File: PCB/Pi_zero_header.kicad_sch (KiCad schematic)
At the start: 95 parts, among them J1 Raspberry_Pi_2_3, J2 USB_C_Receptacle_USB2.0, J3 Screw_Terminal_01x02, J4 Screw_Terminal_01x02, SW1 SW_Push, U1 RP2040, U2 W25Q128JVS, U3 TB6612FNG, U4 TPS630701RNMR, U5 TPS630701RNMR, U6 PQ25792RQMR, Y1 Crystal

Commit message: Hopefully done schema
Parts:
- removed C17, C37, C38, C39, C40: 10u, symbol Device:C
- added J5: Conn_02x04_Top_Bottom, Connector_PinHeader_2.54mm:PinHeader_2x04_P2.54mm_Horizontal, symbol Connector_Generic:Conn_02x04_Top_Bottom
- added J7: Conn_01x04, Connector_PinHeader_2.54mm:PinHeader_1x04_P2.54mm_Horizontal, symbol Connector_Generic:Conn_01x04
- added J8: Conn_02x03_Top_Bottom, Connector_PinHeader_2.54mm:PinHeader_2x03_P2.54mm_Horizontal, symbol Connector_Generic:Conn_02x03_Top_Bottom
- added J9: Conn_01x02, Connector_PinHeader_2.54mm:PinHeader_1x02_P2.54mm_Horizontal, symbol Connector_Generic:Conn_01x02
- added SW2: SW_Push, Button_Switch_SMD:SW_Push_1P1T_NO_Vertical_Wuerth_434133025816, symbol Switch:SW_Push
- added SW3: SW_SPST, Button_Switch_THT:SW_DIP_SPSTx01_Piano_10.8x4.1mm_W7.62mm_P2.54mm, symbol Switch:SW_SPST
- C36: value 10u -> 47u
- R2: value R -> 10k
- Y1: value Crystal -> 12M
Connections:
- net +3V3: now also J5.1 (Pin_1), J5.5 (Pin_5)
- net +5V: now also J7.1 (Pin_1), J8.2 (Pin_2), J8.5 (Pin_5)
- net GND: now also J5.2 (Pin_2), J5.6 (Pin_6), J7.2 (Pin_2), J8.3 (Pin_3), J8.6 (Pin_6), J9.2 (Pin_2), SW2.1
- net SCL_PWR: now also U1.4 (GPIO2)
- net SDA_PWR: now also U1.5 (GPIO3)
- net VDD: now also SW3.2 (B); no longer C35.1, C36.1, U6.25 (SYS)
- net MOSI_RPi: now reaches U1.11 (GPIO8)
- net MOSI_RPi: now also J1.19 (MOSI0/GPIO10)
- net SCLK_RPi: now reaches U1.12 (GPIO9)
- net SCLK_RPi: now also J1.23 (SCLK0/GPIO11)
- net at U1.2 (GPIO0): now also J5.3 (Pin_3), J5.7 (Pin_7)
- net at U1.26 (RUN): now also SW2.2
- net at U1.28 (GPIO17): now also J8.4 (Pin_4)
- net at U1.29 (GPIO18): now also J8.1 (Pin_1)
- net at U1.3 (GPIO1): now also J5.4 (Pin_4), J5.8 (Pin_8)
- net PWMA: now reaches U1.30 (GPIO19)
- net PWMA: now also U3.23 (PWMA)
- net PWMB: now reaches U1.31 (GPIO20)
- net PWMB: now also U3.15 (PWMB)
- net AIN1: now reaches U1.32 (GPIO21)
- net AIN1: now also U3.21 (AIN1)
- net AIN2: now reaches U1.34 (GPIO22)
- net AIN2: now also U3.22 (AIN2)
- net BIN1: now reaches U1.35 (GPIO23)
- net BIN1: now also U3.17 (BIN1)
- net BIN2: now reaches U1.36 (GPIO24)
- net BIN2: now also U3.16 (BIN2)
- net STBY_N: now reaches U1.37 (GPIO25)
- net STBY_N: now also U3.19 (STBY)
- net QSPI_SS: now reaches U1.56 (QSPI_SS)
- net QSPI_SS: now also R1.2, R2.2, U2.1 (~{CS})
- net CE_N_PWR: now reaches U1.6 (GPIO4)
- net CE_N_PWR: now also U6.13 (CE_N)
- net QON_N_PWR: now reaches U1.7 (GPIO5)
- net QON_N_PWR: now also U6.12 (QON_N)
- net CE_N_RPI: now reaches U1.8 (GPIO6)
- net CE_N_RPI: now also J1.24 (~{CE0}/GPIO8)
- net MISO_RPi: now reaches U1.9 (GPIO7)
- net MISO_RPi: now also J1.21 (MISO0/GPIO9)
- net +BATT: now reaches C29.1, C30.1, R6.2, U6.22 (BAT), U6.23 (BAT)
- net +BATT: now also J9.1 (Pin_1)
- net at J1.32 (PWM0/GPIO12): now also J7.3 (Pin_3)
- net at J1.33 (PWM1/GPIO13): now also J7.4 (Pin_4)
- new net: C35.1, C36.1, SW3.1 (A), U6.25 (SYS)
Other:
- note added: "AUDIO"
- note added: "BATTERY"
- note added: "BUCK-BOOST"
- note added: "CHARGER"
- note added: "CRYSTAL"
- note added: "FLASH"
- note added: "I2C"
- note added: "MOTORS"
- note added: "RP2040"
- note added: "RPI ZERO 2"
- note added: "SERVOS"
- note added: "USB-C"
- moved on the sheet: C1, C10, C11, C12, C13, C14, C15, C16, C18, C19, C2, C20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

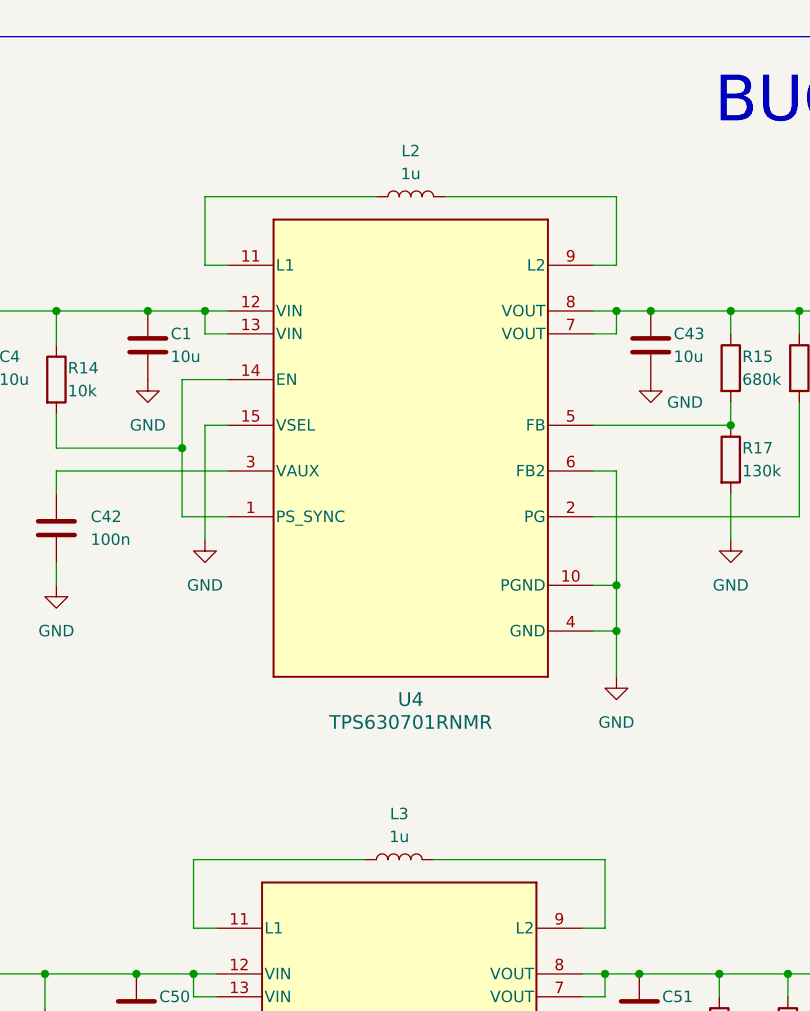
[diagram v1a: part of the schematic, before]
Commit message: Added footprints
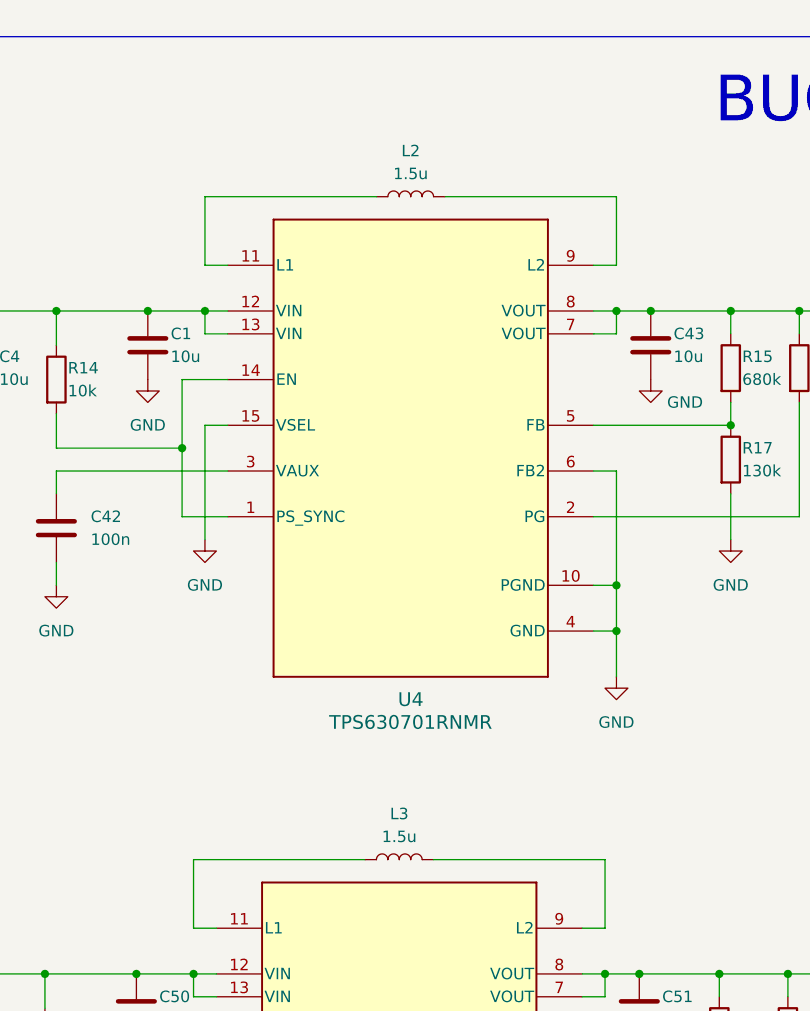
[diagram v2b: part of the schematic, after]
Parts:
- C1, C10, C11, C12, C13, C14, C15, C16, C18, C19, C2, C20, C21, C22, C23, C24, C25, C26, C27, C28, C29, C3, C30, C31, C32, C33, C34, C35, C36, C4, C41, C42, C43, C44, C45, C46, C47, C48, C49, C5, C50, C51, C52, C53, C54, C6, C7, C8, C9: footprint (none) -> Capacitor_SMD:C_0603_1608Metric
- D1: footprint (none) -> LED_SMD:LED_0603_1608Metric
- L1: footprint (none) -> Inductor_SMD:L_0805_2012Metric
- L2, L3: value 1u -> 1.5u; footprint (none) -> Inductor_SMD:L_0805_2012Metric
- R1, R10, R11, R12, R13, R14, R15, R16, R17, R18, R19, R2, R20, R21, R3, R4, R5, R6, R7, R8, R9: footprint (none) -> Resistor_SMD:R_0603_1608Metric
- Y1: footprint (none) -> Crystal:Crystal_SMD_HC49-SD

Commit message: I relized I fucked up...
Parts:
- added D2: LED, LED_SMD:LED_0402_1005Metric, symbol Device:LED
- added J6: Conn_01x07, Connector_PinHeader_2.54mm:PinHeader_1x07_P2.54mm_Vertical, symbol Connector_Generic:Conn_01x07
- added R22: 3k3, Resistor_SMD:R_0402_1005Metric, symbol Device:R
- C1, C10, C11, C12, C13, C14, C15, C16, C18, C19, C2, C20, C21, C22, C23, C24, C25, C26, C27, C28, C29, C3, C30, C31, C32, C33, C34, C35, C36, C4, C41, C42, C43, C44, C45, C46, C47, C48, C49, C5, C50, C51, C52, C53, C54, C6, C7, C8, C9: footprint Capacitor_SMD:C_0603_1608Metric -> Capacitor_SMD:C_0402_1005Metric
- D1: footprint LED_SMD:LED_0603_1608Metric -> LED_SMD:LED_0402_1005Metric
- J5: footprint Connector_PinHeader_2.54mm:PinHeader_2x04_P2.54mm_Horizontal -> Connector_PinHeader_2.54mm:PinHeader_2x04_P2.54mm_Vertical
- J7: footprint Connector_PinHeader_2.54mm:PinHeader_1x04_P2.54mm_Horizontal -> Connector_PinHeader_2.54mm:PinHeader_1x04_P2.54mm_Vertical
- J8: footprint Connector_PinHeader_2.54mm:PinHeader_2x03_P2.54mm_Horizontal -> Connector_PinHeader_2.54mm:PinHeader_2x03_P2.54mm_Vertical
- J9: footprint Connector_PinHeader_2.54mm:PinHeader_1x02_P2.54mm_Horizontal -> Connector_PinHeader_2.54mm:PinHeader_1x02_P2.54mm_Vertical
- R1, R10, R11, R12, R13, R14, R15, R16, R17, R18, R19, R2, R20, R21, R3, R4, R5, R6, R7, R8, R9: footprint Resistor_SMD:R_0603_1608Metric -> Resistor_SMD:R_0402_1005Metric
- SW3: footprint Button_Switch_THT:SW_DIP_SPSTx01_Piano_10.8x4.1mm_W7.62mm_P2.54mm -> Button_Switch_THT:SW_CuK_OS102011MA1QN1_SPDT_Angled
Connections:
- net +3V3: now also J6.1 (Pin_1)
- net GND: now also J6.2 (Pin_2), R22.2
- net at U1.13 (GPIO10): now also J6.3 (Pin_3)
- net at U1.14 (GPIO11): now also J6.4 (Pin_4)
- net at U1.15 (GPIO12): now also J6.5 (Pin_5)
- net at U1.16 (GPIO13): now also J6.6 (Pin_6)
- net at U1.17 (GPIO14): now also J6.7 (Pin_7)
- net at U1.18 (GPIO15): now also D2.1 (K)
- new net: D2.2 (A), R22.1
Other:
- note added: "SPI"
- moved on the sheet: J5

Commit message: Updated PCB design
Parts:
- removed J7: Conn_01x04, Connector_PinHeader_2.54mm:PinHeader_1x04_P2.54mm_Vertical, symbol Connector_Generic:Conn_01x04
- removed Y1: 12M, Crystal:Crystal_SMD_HC49-SD, symbol Device:Crystal
- added Y2: 12M, Crystal:Crystal_SMD_3225-4Pin_3.2x2.5mm, symbol Device:Crystal_GND24
- C1, C19, C21, C24, C25, C27, C28, C29, C30, C4, C41, C43, C47, C48, C50, C51: footprint Capacitor_SMD:C_0402_1005Metric -> Capacitor_SMD:C_0805_2012Metric
- C2, C3: value 27p -> 15p
- C34, C44, C45, C46, C52, C53, C54: footprint Capacitor_SMD:C_0402_1005Metric -> Capacitor_SMD:C_0603_1608Metric
- C36: footprint Capacitor_SMD:C_0402_1005Metric -> Capacitor_SMD:C_1206_3216Metric
- L1, L2, L3: footprint Inductor_SMD:L_0805_2012Metric -> Inductor_SMD:L_1008_2520Metric
- SW3: footprint Button_Switch_THT:SW_CuK_OS102011MA1QN1_SPDT_Angled -> Button_Switch_SMD:SW_SPDT_PCM12
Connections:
- net GND: now also Y2.2, Y2.4
- net XIN: now also Y2.3
- net at C3.1, R5.1: now also Y2.1
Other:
- note removed: "AUDIO"
- moved on the sheet: R5

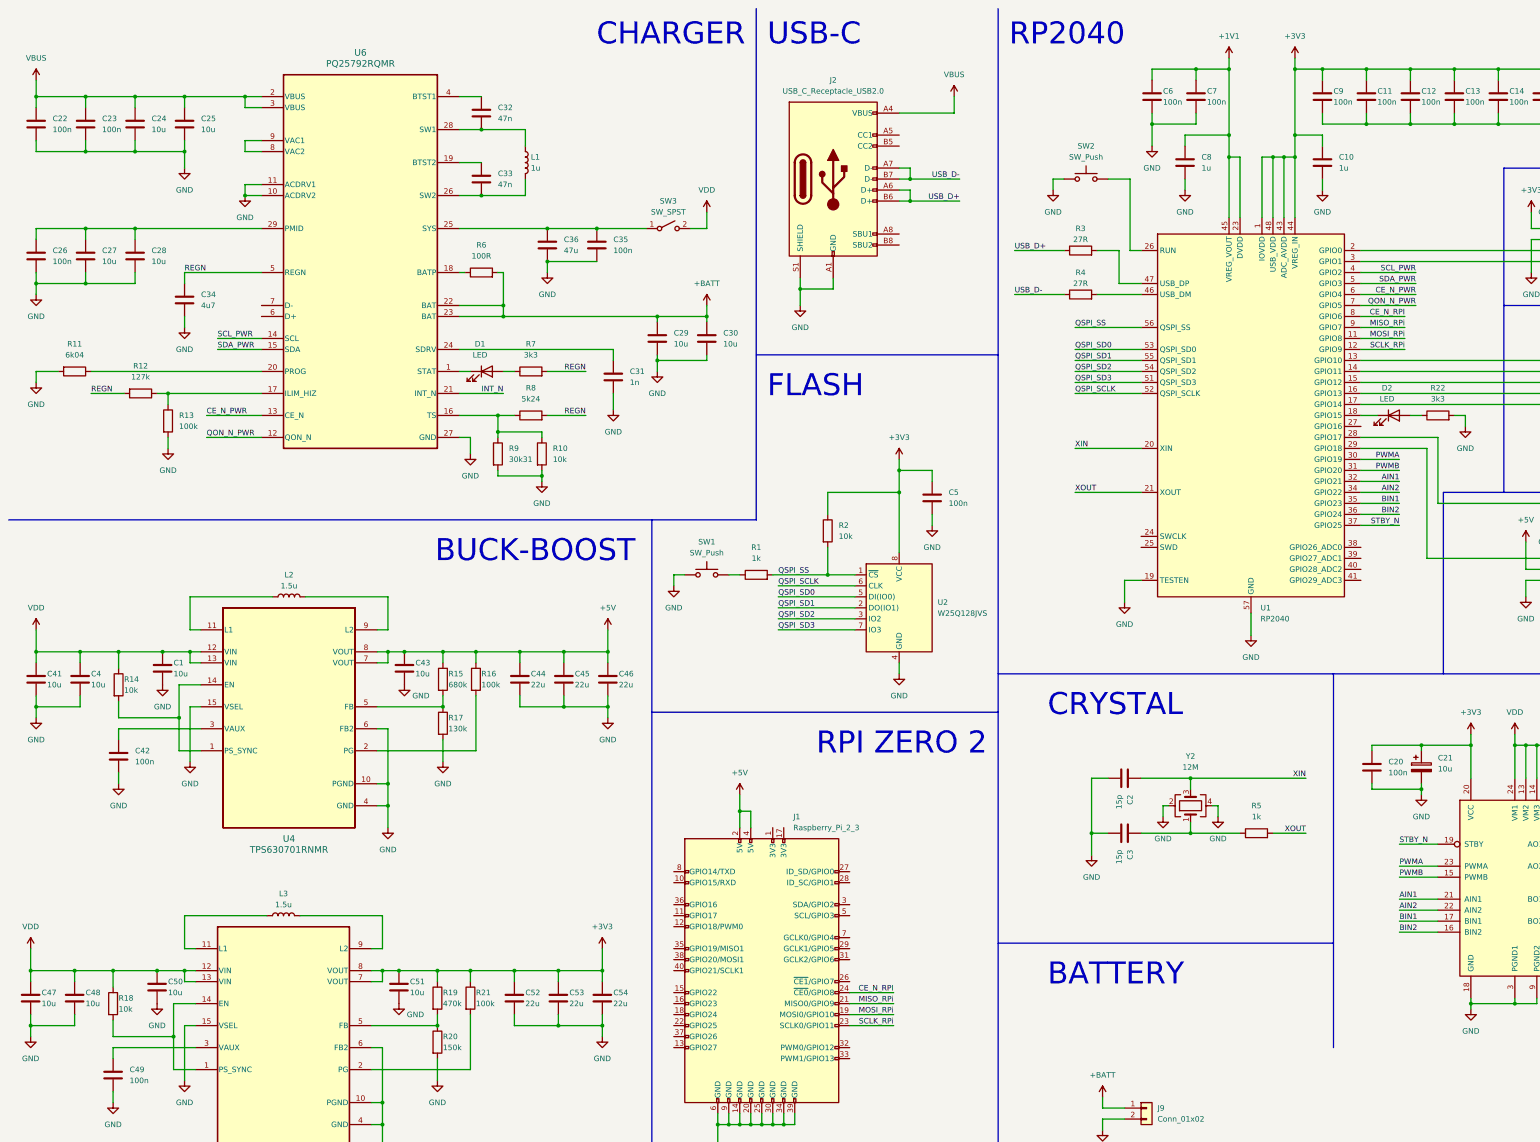
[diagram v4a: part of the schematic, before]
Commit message: I will need different buck-boost...
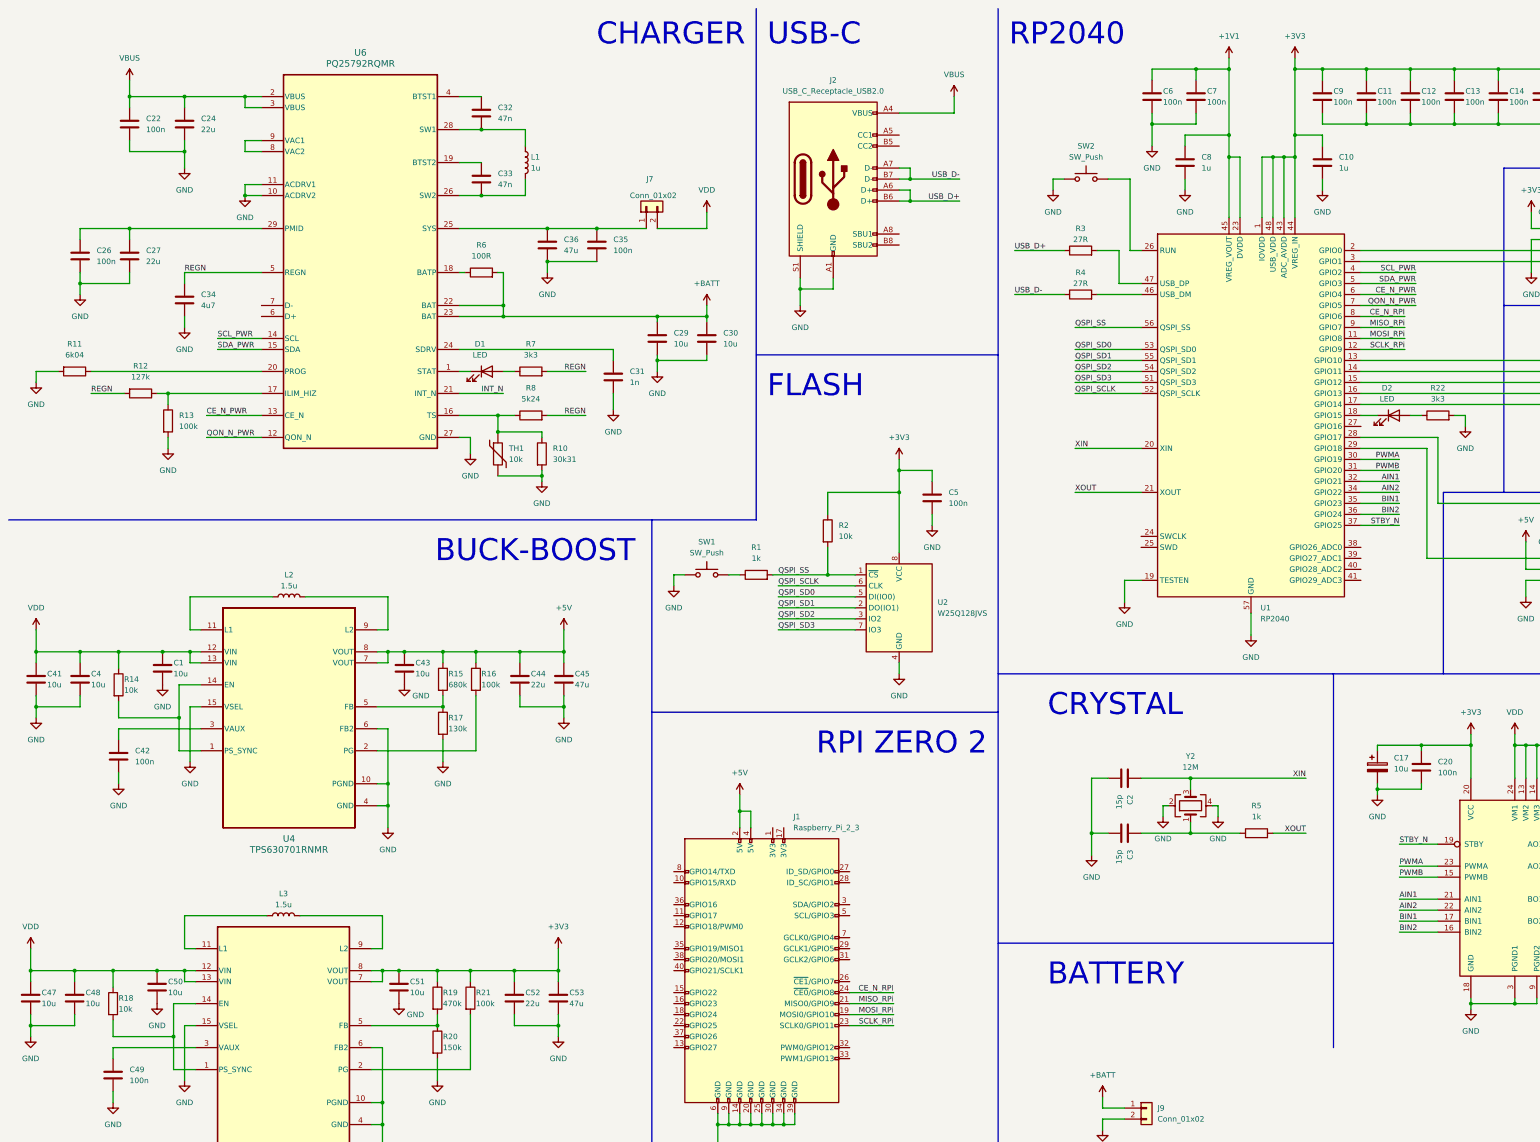
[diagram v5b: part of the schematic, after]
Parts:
- removed C21: 10u, Capacitor_SMD:C_0805_2012Metric, symbol Device:C_Polarized
- removed C23: 100n, Capacitor_SMD:C_0402_1005Metric, symbol Device:C
- removed C25, C28: 10u, Capacitor_SMD:C_0805_2012Metric, symbol Device:C
- removed C46, C54: 22u, Capacitor_SMD:C_0603_1608Metric, symbol Device:C
- removed R9: 30k31, Resistor_SMD:R_0402_1005Metric, symbol Device:R
- removed SW3: SW_SPST, Button_Switch_SMD:SW_SPDT_PCM12, symbol Switch:SW_SPST
- added C17: 10u, Capacitor_Tantalum_SMD:CP_EIA-3216-18_Kemet-A, symbol Device:C_Polarized
- added J7: Conn_01x02, Connector_PinHeader_2.54mm:PinHeader_1x02_P2.54mm_Vertical, symbol Connector_Generic:Conn_01x02
- added TH1: 10k, Resistor_THT:R_Axial_DIN0204_L3.6mm_D1.6mm_P2.54mm_Vertical, symbol Device:Thermistor
- C1, C43, C50: footprint Capacitor_SMD:C_0805_2012Metric -> Capacitor_SMD:C_0603_1608Metric
- C19: footprint Capacitor_SMD:C_0805_2012Metric -> Capacitor_Tantalum_SMD:CP_EIA-3216-18_Kemet-A
- C24, C27: value 10u -> 22u
- C44, C52: footprint Capacitor_SMD:C_0603_1608Metric -> Capacitor_SMD:C_0805_2012Metric
- C45, C53: value 22u -> 47u; footprint Capacitor_SMD:C_0603_1608Metric -> Capacitor_SMD:C_0805_2012Metric
- R10: value 10k -> 30k31
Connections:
- net +3V3: now also C17.1
- net GND: now also C17.2, TH1.2
- net VDD: now also J7.2 (Pin_2)
- net at R10.1, R8.1, U6.16 (TS): now also TH1.1
- net at C35.1, C36.1, U6.25 (SYS): now also J7.1 (Pin_1)
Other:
- moved on the sheet: C20, C22, C24, C26, C27
